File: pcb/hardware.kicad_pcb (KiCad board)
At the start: 4 copper layers, 162 parts, among them J1 Micro_SD_Card_Det_Hirose_DM3AT, J2 USB_A, J3 USB_A, U1 AS4C512M16D3L-12BIN, U2 A33, U3 TPS62095RGTR, U4 TPS62095RGTR, U5 TPS62095RGTR, U6 TPS62095RGTR, U7 AP131-25, U8 MPM-15-5, Y1 24Mhz, Y2 32.768khz

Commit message: Working on the power supplies
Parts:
- removed C35, C36, C39, C41, C44, C45, C47, C49, C51, C52, C63: 100nF, Capacitor_SMD:C_0402_1005Metric
- removed C57, C58, C71: 22uF, Capacitor_SMD:C_0402_1005Metric
- removed TP10, TP2, TP5, TP9: TestPoint, TestPoint:TestPoint_Pad_1.0x1.0mm
- C10, C11, C14, C15, C16, C17, C22, C23, C24, C25, C26, C28, C6, C9: footprint Capacitor_SMD:C_0402_1005Metric -> Capacitor_SMD:C_0805_2012Metric
- C31, C37, C53, C59, C61, C65, C67: moved to B.Cu
- C55, C69: value 100nF -> 22uF; moved to B.Cu
- C56: value 100nF -> 22uF
- moved C99 84.9 mm to (108.7, 95.5)
- moved R32 80.6 mm to (106.4, 109.3)
- moved C103 75.0 mm to (106.4, 106.4), turned to 180 degrees
- moved C106 71.5 mm to (131.7, 40.6)
- moved C100 71.5 mm to (101.4, 94.0), turned to 180 degrees
- moved C104 71.2 mm to (106.4, 105.4), turned to 180 degrees
- moved C6 69.9 mm to (79.1, 79.6), turned to 90 degrees
- moved R31 68.1 mm to (101.4, 95.1)
- moved C105 68.0 mm to (132.0, 49.7)
- moved C8 67.9 mm to (78.5, 83.4), turned to 270 degrees
- moved C101 67.7 mm to (106.4, 110.4), turned to 180 degrees
- moved TP1 64.2 mm to (48.2, 57.8)
- moved C37 63.8 mm to (118.0, 105.7)
- moved U3 62.0 mm to (75.8, 82.2)
- moved C7 61.8 mm to (76.4, 84.9)
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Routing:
- net +1V1: track 0.00 -> 11.9 mm, vias 1 -> 6
- net +3V0: track 0.00 -> 6.38 mm, vias 0 -> 2
- net GND: vias 13 -> 22

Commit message: Working on the routing.
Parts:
- removed C60, C62: 100nF, Capacitor_SMD:C_0402_1005Metric
- removed C72: 22uF, Capacitor_SMD:C_0402_1005Metric
- C64, C66, C68, C99, R30: moved to B.Cu
- C70: value 100nF -> 22uF; moved to B.Cu
- moved C64 29.9 mm to (116.6, 104.3), turned to 90 degrees
- moved C66 23.2 mm to (110.5, 107.7), turned to 180 degrees
- moved C70 23.1 mm to (110.5, 111.7), turned to 90 degrees
- moved C68 21.6 mm to (111.5, 111.7), turned to 90 degrees
- moved C61 15.7 mm to (100.9, 100.1)
- moved C100 13.3 mm to (106.6, 106.2), turned to 0 degrees
- moved R30 12.1 mm to (110.1, 104.5), turned to 180 degrees
- moved C4 11.7 mm to (112.9, 101.3)
- moved C5 11.7 mm to (114.8, 101.3)
- moved R4 11.7 mm to (112.9, 100.3)
- moved R5 11.7 mm to (114.8, 100.3)
- moved C99 11.4 mm to (110.0, 106.7), turned to 180 degrees
- moved R31 11.3 mm to (106.6, 105.1), turned to 180 degrees
- moved C103 3.12 mm to (106.6, 109.5)
- moved C104 3.11 mm to (106.6, 108.5)
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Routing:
- net /DVREF: track 0.00 -> 11.3 mm, vias 0 -> 2
- net Net-(C97-Pad1): track 0.00 -> 7.19 mm
- net Net-(C98-Pad1): track 0.00 -> 6.49 mm
- net Net-(C96-Pad2): track 0.00 -> 5.20 mm
- net Net-(C102-Pad1): track 0.00 -> 4.52 mm
- net Net-(C95-Pad2): track 0.00 -> 4.13 mm
- net Net-(C103-Pad1): track 0.00 -> 3.94 mm
- net +1V1: track 11.9 -> 15.4 mm, vias 6 -> 5
- net Net-(C101-Pad1): track 0.00 -> 3.44 mm
- net +3V0: track 6.38 -> 9.79 mm, vias 2 -> 3
- net /HPVCCBP: track 0.00 -> 3.37 mm
- net +3V3: track 0.00 -> 2.83 mm, vias 0 -> 2
- net Net-(C100-Pad2): track 0.00 -> 2.41 mm
- net /VCC-EFUSE: track 0.00 -> 1.35 mm, vias 0 -> 1
- net Net-(C99-Pad1): track 0.00 -> 1.34 mm, vias 0 -> 1

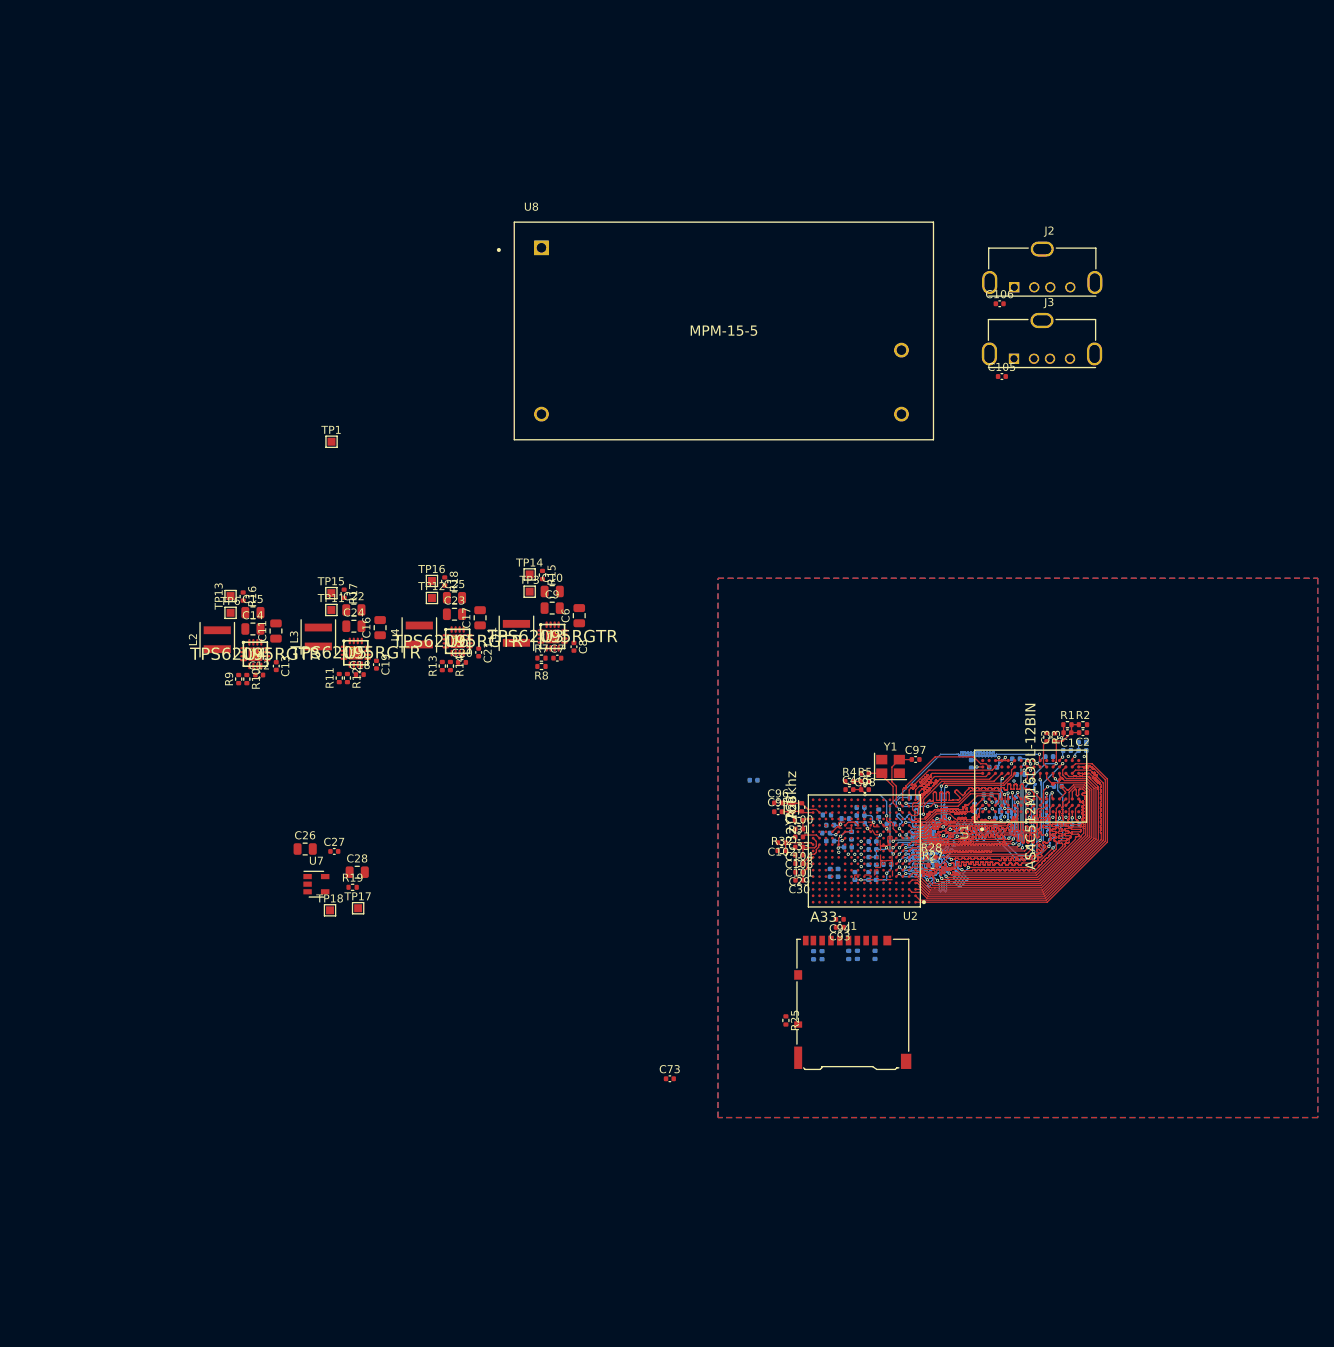
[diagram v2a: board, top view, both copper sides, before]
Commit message: Routing power supplies
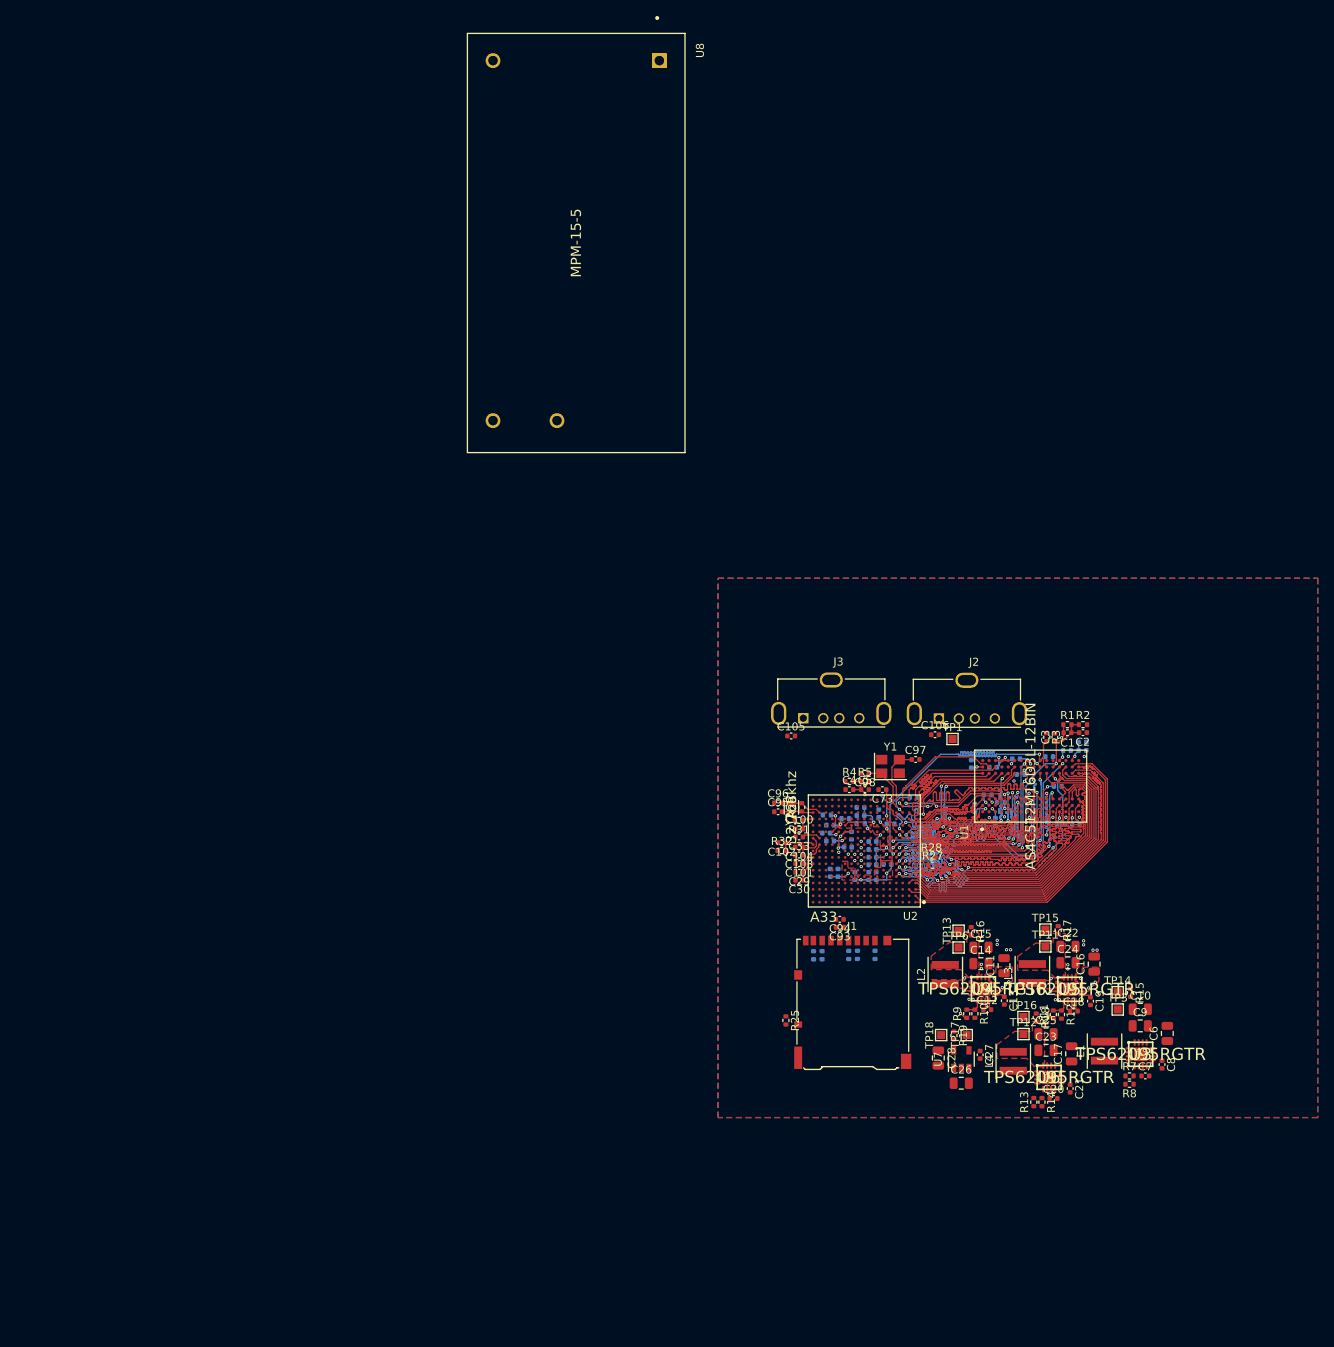
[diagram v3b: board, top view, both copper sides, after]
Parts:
- removed C61: 100nF, Capacitor_SMD:C_0402_1005Metric
- moved C12 100.2 mm to (130.1, 128.8)
- moved C13 100.2 mm to (132.3, 127.7)
- moved R9 100.2 mm to (127.6, 129.3)
- moved TP13 100.2 mm to (126.5, 118.9)
- moved TP6 100.2 mm to (126.5, 121.0)
- moved C11 100.2 mm to (132.2, 123.3)
- moved C14 100.2 mm to (129.3, 123.1)
- moved C15 100.2 mm to (129.3, 121.0)
- moved L2 100.2 mm to (124.9, 124.4)
- moved R10 100.2 mm to (128.6, 129.3)
- moved R16 100.2 mm to (128.1, 119.0)
- moved U4 100.2 mm to (129.6, 126.2)
- moved C16 98.7 mm to (143.5, 123.1)
- moved C19 98.7 mm to (143.0, 127.7)
- moved C24 98.7 mm to (140.2, 122.9)
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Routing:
- net +5V: track 0.00 -> 10.9 mm, vias 0 -> 10
- net Net-(C14-Pad1): track 0.00 -> 7.29 mm, vias 0 -> 2
- net Net-(C22-Pad1): track 0.00 -> 6.90 mm, vias 0 -> 2
- net +2V5: track 0.00 -> 5.03 mm
- net +3V3: track 2.83 -> 5.28 mm, vias 2 -> 3
- net Net-(R11-Pad2): track 0.00 -> 2.31 mm
- net Net-(R10-Pad1): track 0.00 -> 2.27 mm
- net Net-(R30-Pad1): track 0.00 -> 1.96 mm, vias 0 -> 1
- net +1V35: track 39.5 -> 40.9 mm, vias 18 -> 19
- net Net-(C18-Pad2): track 0.00 -> 1.35 mm
- net Net-(C18-Pad1): track 0.00 -> 1.35 mm
- net Net-(C13-Pad1): track 0.00 -> 1.25 mm
- net Net-(C12-Pad1): track 0.00 -> 1.23 mm
- net Net-(C12-Pad2): track 0.00 -> 1.22 mm
- net Net-(C19-Pad1): track 0.00 -> 1.21 mm
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- added copper zone on F.Cu, net +3V3
- added copper zone on F.Cu, net +5V
- added copper zone on F.Cu, net Net-(C14-Pad1)
- added copper zone on F.Cu, net Net-(C22-Pad1)
- added copper zone on F.Cu, net Net-(C23-Pad1)
- added copper zone on F.Cu, net Net-(L2-Pad1)
- added copper zone on F.Cu, net Net-(L3-Pad1)

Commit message: Working on silkscreen/placement
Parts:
- removed U8: MPM-15-5, MPM-15-5:MEAN_WELL-MPM-15-5-MFG
- added H1: MountingHole, MountingHole:MountingHole_3.2mm_M3, F.Cu at (100.0, 132.0)
- added H2: MountingHole, MountingHole:MountingHole_3.2mm_M3, F.Cu at (149.0, 132.0)
- added H3: MountingHole, MountingHole:MountingHole_3.2mm_M3, F.Cu at (100.0, 88.8)
- added H4: MountingHole, MountingHole:MountingHole_3.2mm_M3, F.Cu at (149.0, 89.0)
- added J5: Conn_02x10_Odd_Even, Connector_PinHeader_2.54mm:PinHeader_2x10_P2.54mm_Vertical, F.Cu at (98.4, 97.7)
- moved R8 28.4 mm to (148.0, 109.7), turned to 0 degrees
- moved R7 28.3 mm to (148.0, 108.7), turned to 180 degrees
- moved C7 27.7 mm to (146.0, 109.6), turned to 180 degrees
- moved C8 25.9 mm to (143.9, 111.0), turned to 90 degrees
- moved U3 22.2 mm to (146.6, 112.3), turned to 180 degrees
- moved L1 20.6 mm to (151.1, 114.4), turned to 270 degrees
- moved C6 19.3 mm to (143.2, 114.9), turned to 270 degrees
- moved C9 15.5 mm to (146.8, 115.5), turned to 180 degrees
- moved R13 11.6 mm to (129.0, 131.0), turned to 0 degrees
- moved R14 11.5 mm to (129.0, 132.1), turned to 180 degrees
- moved TP3 11.5 mm to (149.9, 117.8), turned to 180 degrees
- moved C10 11.4 mm to (146.8, 117.6), turned to 180 degrees
- moved C20 11.0 mm to (129.5, 133.5), turned to 270 degrees
- moved C21 10.2 mm to (130.7, 135.6), turned to 180 degrees
- moved TP14 7.54 mm to (149.9, 119.9), turned to 180 degrees
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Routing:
- net +5V: track 10.9 -> 21.7 mm, vias 10 -> 20
- net Net-(C10-Pad1): track 0.00 -> 7.31 mm, vias 0 -> 2
- net Net-(C23-Pad1): track 0.00 -> 7.29 mm, vias 0 -> 2
- net +1V1: track 15.4 -> 18.2 mm
- net Net-(R7-Pad2): track 0.00 -> 2.17 mm
- net +1V35: track 40.9 -> 42.7 mm, vias 19 -> 26
- net Net-(C22-Pad1): track 6.90 -> 8.53 mm
- net Net-(C7-Pad2): track 0.00 -> 1.36 mm
- net Net-(C7-Pad1): track 0.00 -> 1.29 mm
- net Net-(C8-Pad1): track 0.00 -> 1.21 mm
- net GND: vias 38 -> 54
- added copper zone on F.Cu, net Net-(C10-Pad1)
- added copper zone on F.Cu, net Net-(L1-Pad1)
- added copper zone on F.Cu, net Net-(L4-Pad1)
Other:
- board outline added: 59 x 53 mm
